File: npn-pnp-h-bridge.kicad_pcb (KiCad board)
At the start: 2 copper layers, 44.2 x 18.4 mm, 35 parts, among them J1 S4B-PH-K-S_LF__SN_, J2 S2B-PH-K-S_LF__SN_, Q1 MMBT3904, Q2 MMBT3904, Q3 MMBT3904, Q4 MMBT3904

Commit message: some small touchups
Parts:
- moved C1 1.00 mm to (151.2, 91.5)
- moved C2 1.00 mm to (155.6, 91.5)
- moved R1 1.00 mm to (153.4, 91.5)
- moved R2 1.00 mm to (157.8, 91.5)
- moved R3 1.00 mm to (160.2, 91.5)
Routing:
- net /bQ2: track 9.85 -> 8.91 mm
- net VDD: track 52.5 -> 53.1 mm
- net GND: vias 14 -> 20

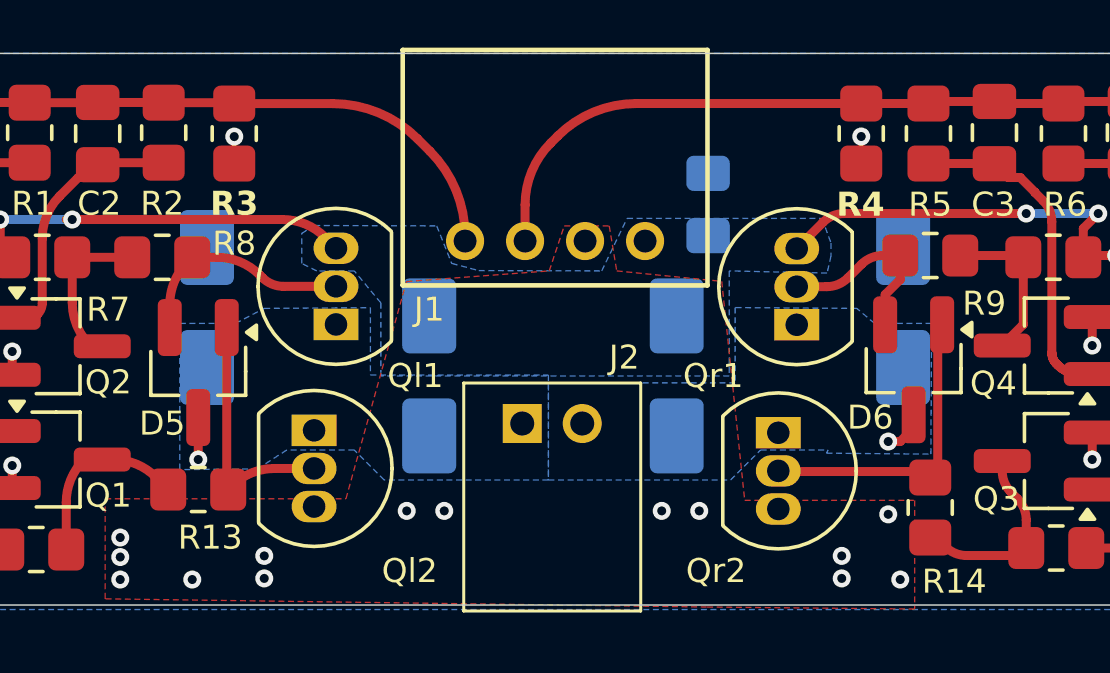
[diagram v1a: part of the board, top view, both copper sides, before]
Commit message: Use handsoldering-footprints for diodes
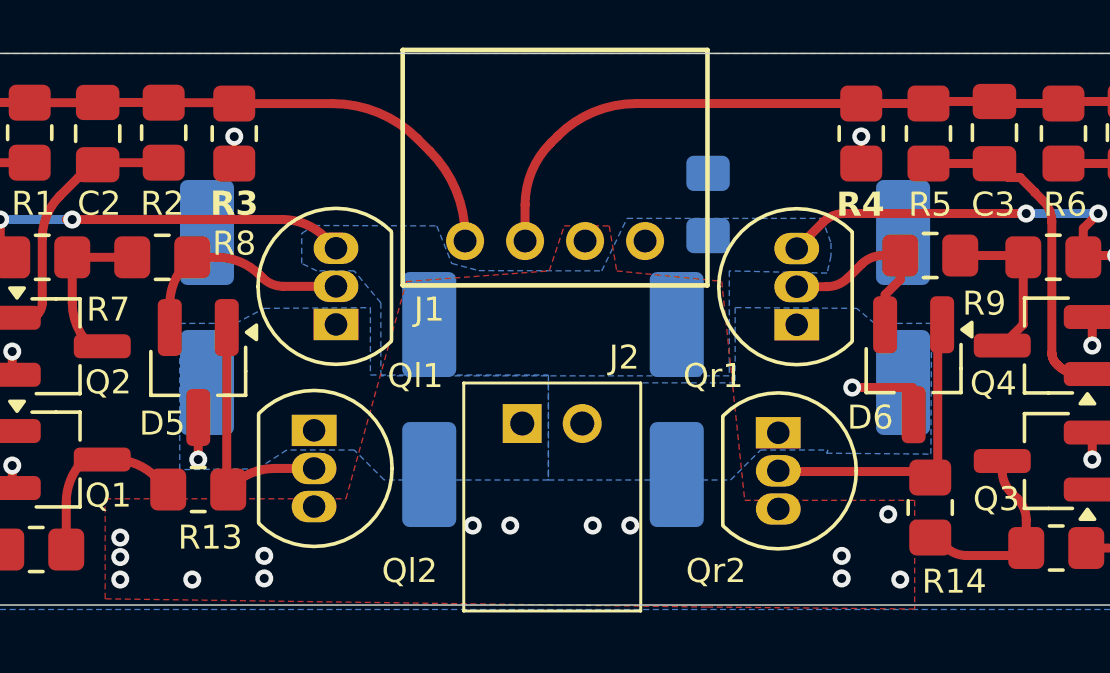
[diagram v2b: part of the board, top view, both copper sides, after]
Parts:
- D1, D2, D3, D4: footprint Diode_SMD:D_SMA -> Diode_SMD:D_SMA_Handsoldering
- moved D1 0.79 mm to (166.7, 100.4)
- moved D2 0.79 mm to (174.9, 100.4)
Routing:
- net /O2: track 1.65 -> 2.88 mm

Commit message: beautify schematic
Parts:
- added MH1: ToolingHole_1.152mm, MountingHole:ToolingHole_1.152mm, F.Cu at (162.8, 92.2)
- added MH2: ToolingHole_1.152mm, MountingHole:ToolingHole_1.152mm, F.Cu at (178.6, 92.2)
- R13, R14: value 180 -> 100
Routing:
- net /L_IN: track 19.4 -> 20.4 mm
- net /R_IN: track 23.2 -> 24.0 mm

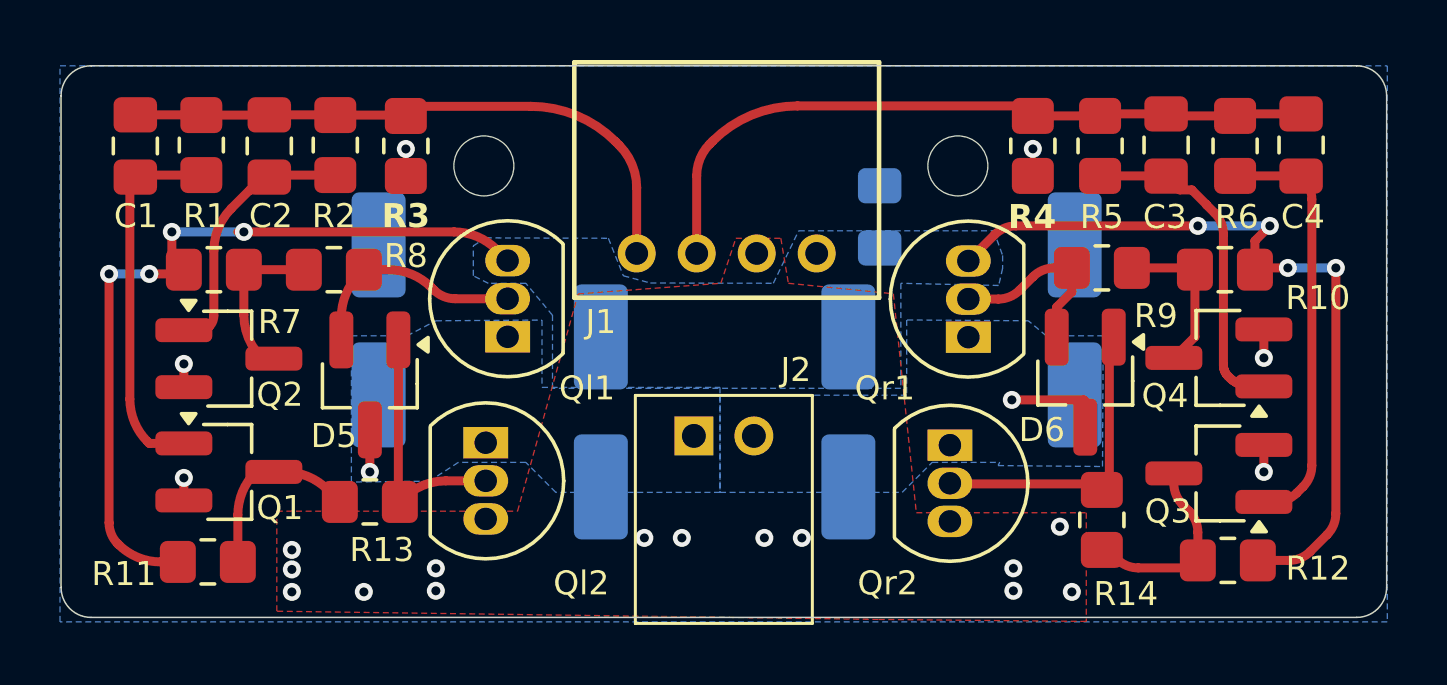
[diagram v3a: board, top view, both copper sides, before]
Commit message: Changed MMBT3904 for a dual-NPN MMDT3904 for miniturization
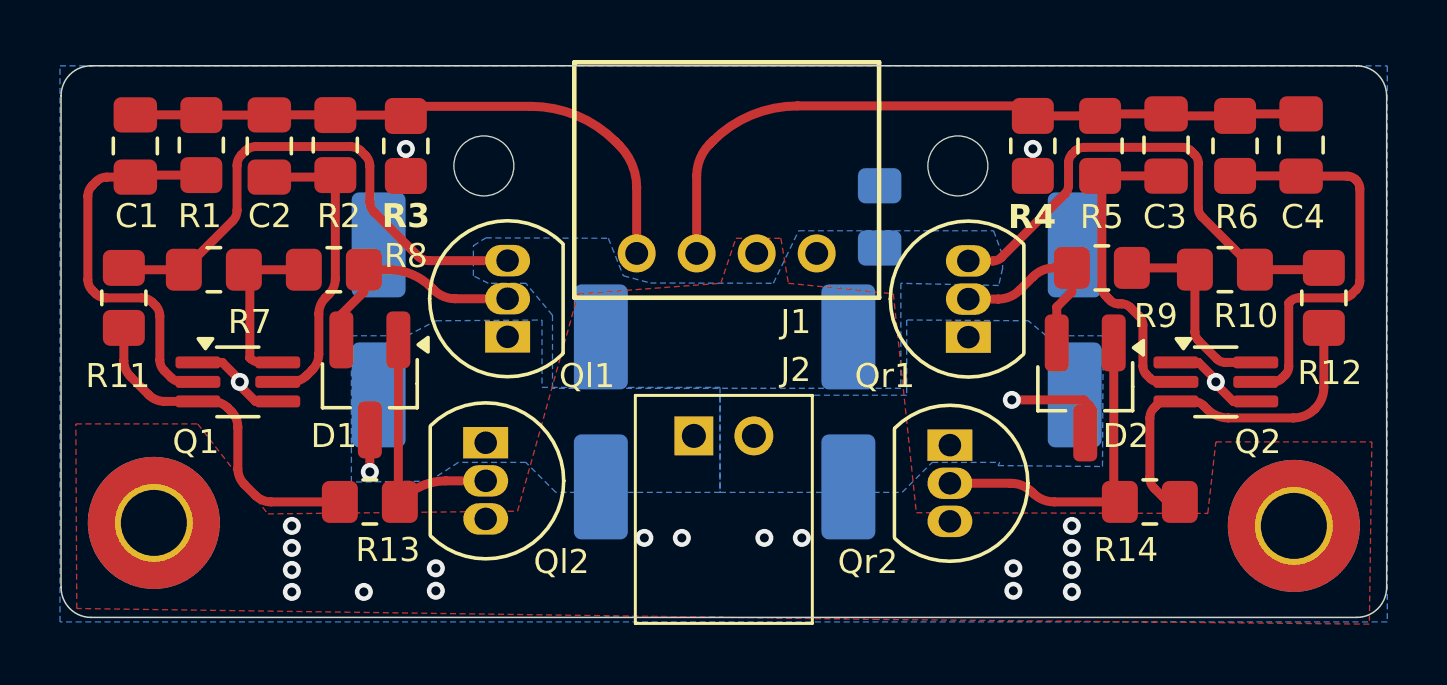
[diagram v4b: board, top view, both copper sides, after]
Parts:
- removed Q3, Q4: MMBT3904, Package_TO_SOT_SMD:SOT-23_Handsoldering
- added H1: MountingHole_Pad, MountingHole:MountingHole_2.2mm_M2_Pad_TopBottom, F.Cu at (151.8, 104.1)
- added H2: MountingHole_Pad, MountingHole:MountingHole_2.2mm_M2_Pad_TopBottom, F.Cu at (189.8, 104.2)
- Q1, Q2: value MMBT3904 -> MMDT3904; footprint Package_TO_SOT_SMD:SOT-23_Handsoldering -> Package_TO_SOT_SMD:SOT-363_SC-70-6_Handsoldering
- moved Q2 32.9 mm to (187.2, 99.4)
- moved R12 9.32 mm to (190.8, 96.6), turned to 90 degrees
- moved R11 9.23 mm to (150.8, 96.6), turned to 90 degrees
- moved C1 4.47 mm to (151.2, 91.5)
- moved C2 4.47 mm to (155.6, 91.5)
- moved R1 4.47 mm to (153.4, 91.5)
- moved R2 4.47 mm to (157.8, 91.5)
- moved Q1 3.01 mm to (154.6, 99.4)
- moved R14 1.71 mm to (185.0, 103.4), turned to 0 degrees
- moved D2 0.19 mm to (182.8, 99.6)
- renumbered C2 to C1, C1 to C2, D5 to D1, D6 to D2, D4 to D3, D3 to D4, D2 to D5, D1 to D6, R2 to R1, R1 to R2
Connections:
- Q1 pad 1: /bQ1 -> GND
- Q1 pad 2: GND -> /bQ2
- Q2 pad 1: /bQ2 -> GND
- Q2 pad 2: GND -> /bQ4
- Q2 pad 3: Net-(Q2-C) -> Net-(Q2B-C2)
- R10 pad 1: Net-(Q4-C) -> Net-(Q2A-C1)
- R12 pad 1: Net-(Q3-C) -> Net-(Q2B-C2)
- R14 pad 2: Net-(Q3-C) -> Net-(Q2B-C2)
- R7 pad 1: Net-(Q2-C) -> Net-(Q1A-C1)
- R8 pad 1: Net-(Q2-C) -> Net-(Q1A-C1)
- R9 pad 2: Net-(Q4-C) -> Net-(Q2A-C1)
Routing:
- net VDD: track 53.1 -> 34.7 mm, vias 8 -> 0
- net Net-(Q2B-C2): track 0.00 -> 12.2 mm
- net Net-(Q2A-C1): track 0.00 -> 6.71 mm
- net Net-(Q3-C): track 6.64 -> 0.00 mm
- net Net-(Q1A-C1): track 0.00 -> 5.97 mm
- net Net-(Q2-C): track 5.50 -> 0.00 mm
- net Net-(Q4-C): track 5.36 -> 0.00 mm
- net Net-(Q1B-C2): track 6.27 -> 11.4 mm
- net /bQ2: track 8.91 -> 13.1 mm
- net GND: track 5.17 -> 8.39 mm, vias 20 -> 21
- net /bQ1: track 12.5 -> 10.2 mm
- net /L2b: track 10.4 -> 11.2 mm
- net /bQ3: track 14.2 -> 13.7 mm

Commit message: fine tuning
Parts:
- moved J1 0.92 mm to (173.9, 94.2)
- moved R14 0.80 mm to (184.2, 103.4)
- moved J2 0.80 mm to (169.8, 102.0)
- moved C5 0.33 mm to (176.2, 93.6)
- moved MH1 0.20 mm to (162.6, 92.2)
- moved MH2 0.20 mm to (178.8, 92.2)
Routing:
- net /O2: track 3.28 -> 1.93 mm
- net /R_IN: track 24.0 -> 23.1 mm
- net /L_IN: track 20.4 -> 19.5 mm
- net Net-(Q2B-C2): track 12.2 -> 11.7 mm
- net GND: vias 21 -> 18

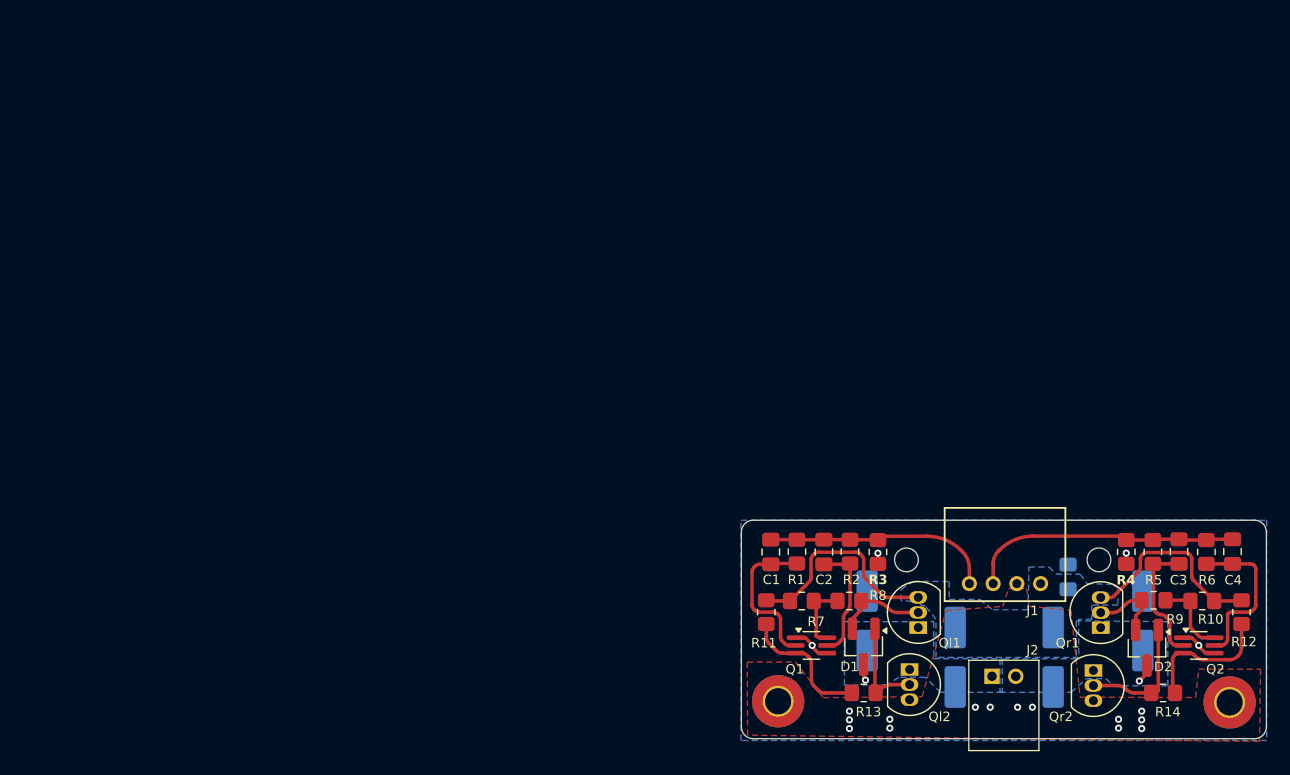
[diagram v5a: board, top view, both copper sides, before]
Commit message: more fine tuning; round board size
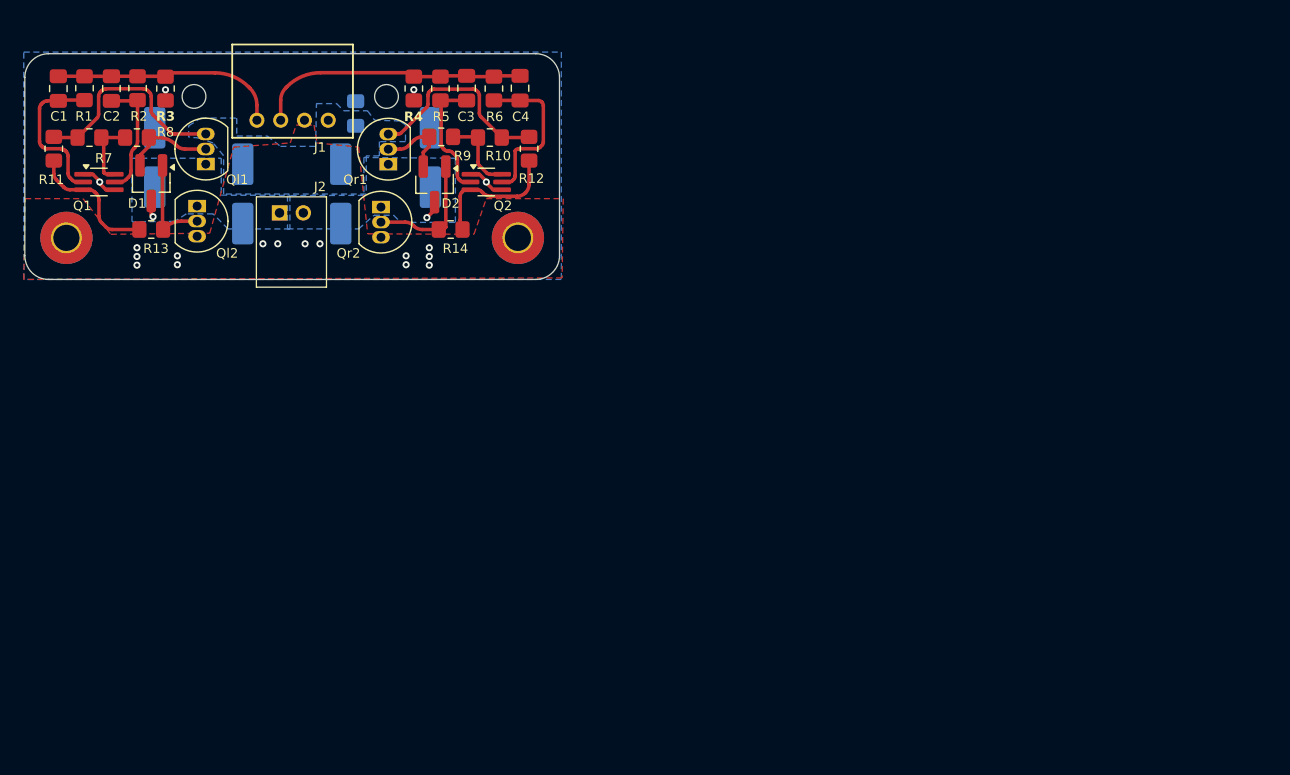
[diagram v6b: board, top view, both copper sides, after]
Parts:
- moved H2 71.5 mm to (129.9, 65.1)
- moved C3 71.5 mm to (125.6, 52.5)
- moved J2 71.5 mm to (109.8, 63.0)
- moved MH2 71.5 mm to (118.8, 53.2)
- moved C1 71.5 mm to (91.2, 52.5)
- moved C2 71.5 mm to (95.7, 52.5)
- moved C4 71.5 mm to (130.1, 52.5)
- moved D1 71.5 mm to (99.0, 60.5)
- moved D3 71.5 mm to (122.5, 58.3)
- moved MH1 71.5 mm to (102.6, 53.2)
- moved Q1 71.5 mm to (94.6, 60.4)
- moved Ql1 71.5 mm to (103.6, 58.9)
- moved R10 71.5 mm to (127.5, 56.7)
- moved R11 71.5 mm to (90.8, 57.6)
- moved R12 71.5 mm to (130.8, 57.6)
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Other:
- board size 44.2 x 18.4 mm -> 45 x 19 mm

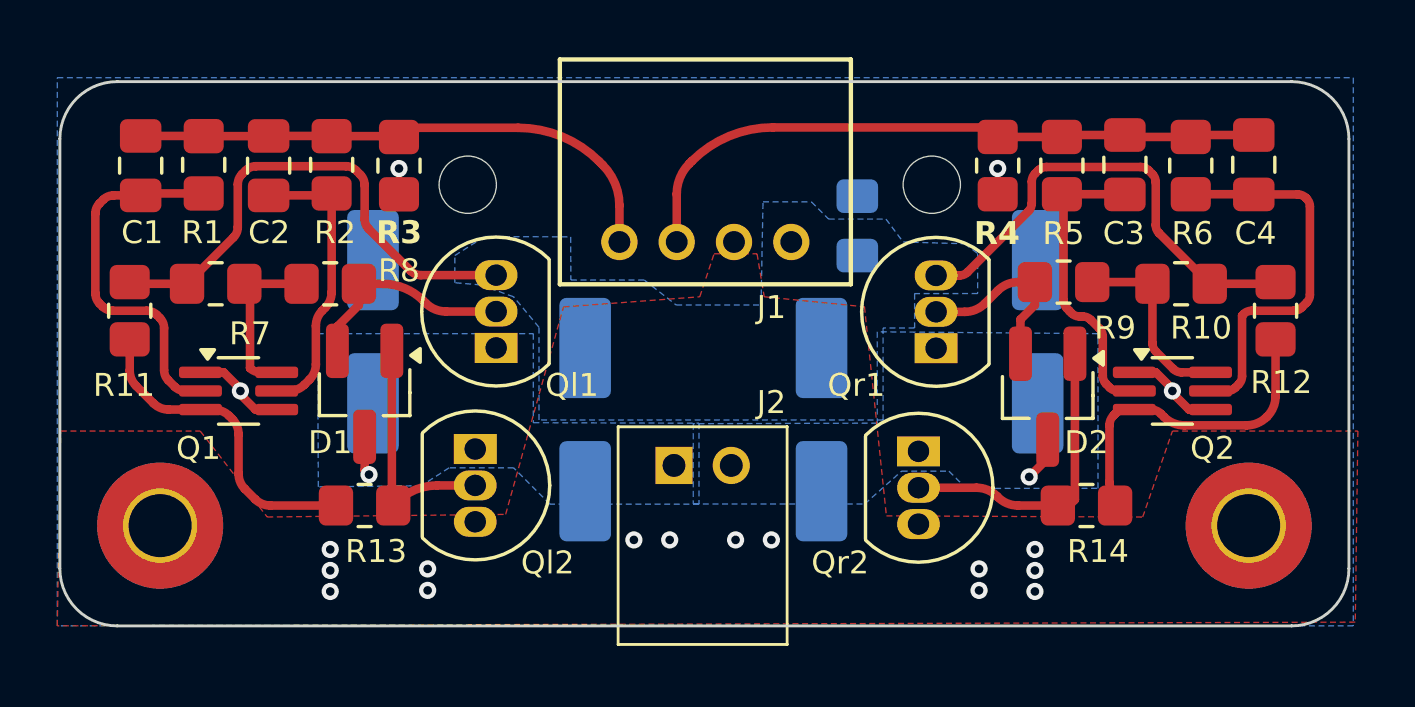
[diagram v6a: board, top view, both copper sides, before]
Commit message: final touches for dual-npn-package
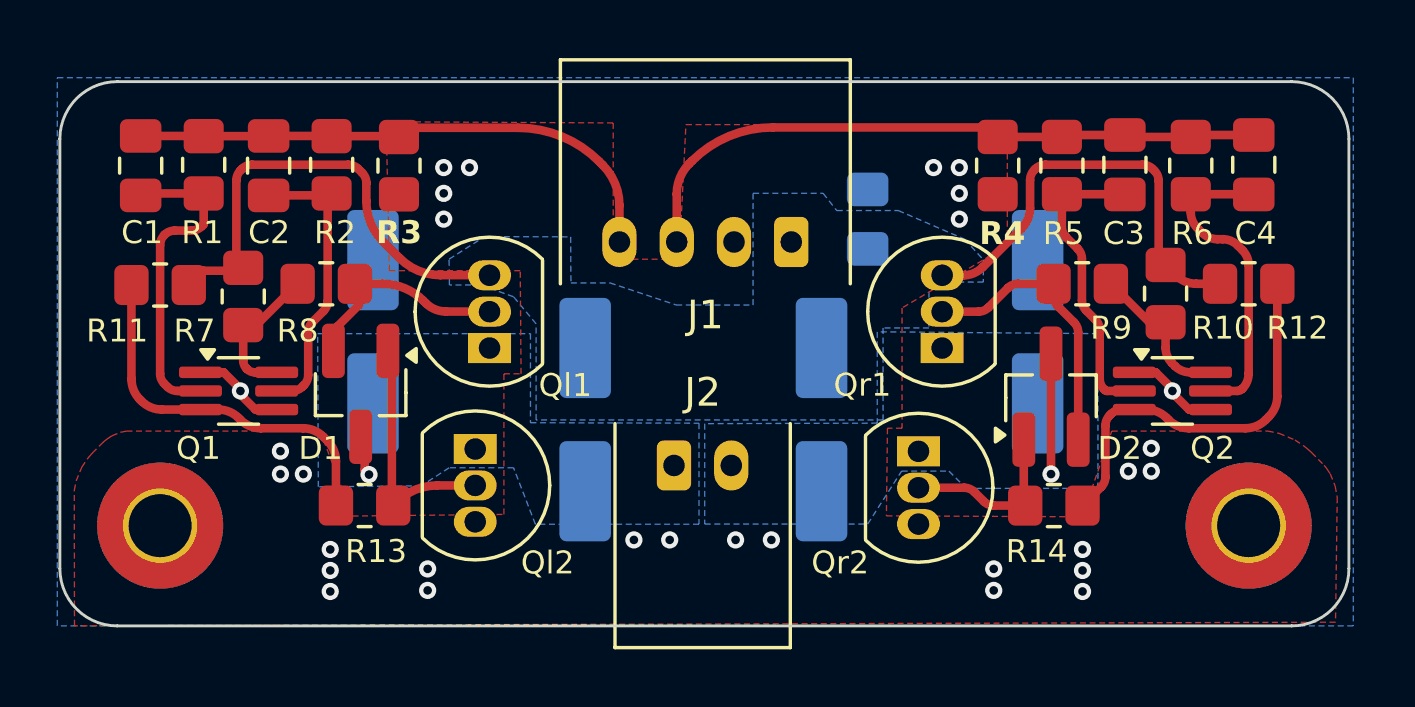
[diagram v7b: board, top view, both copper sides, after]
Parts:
- removed MH1, MH2: ToolingHole_1.152mm, MountingHole:ToolingHole_1.152mm
- J1: footprint Misc:CONN_S4B-PH-K-S_JST -> Misc:JST_PH_S4B-PH-K_1x04_P2.00mm_Horizontal
- J2: footprint Misc:DS2BPHKSLFSN -> Misc:JST_PH_S2B-PH-K_1x02_P2.00mm_Horizontal
- moved R11 1.39 mm to (91.9, 56.7), turned to 0 degrees
- moved R12 1.33 mm to (129.9, 56.7), turned to 180 degrees
- moved R14 1.14 mm to (123.1, 64.4)
- moved R7 1.06 mm to (94.8, 57.1), turned to 90 degrees
- moved R9 0.65 mm to (124.1, 56.7)
- moved R10 0.64 mm to (127.0, 57.0), turned to 90 degrees
- moved C5 0.43 mm to (116.6, 54.4)
- moved Ql1 0.23 mm to (103.4, 58.9)
- moved Qr1 0.21 mm to (119.2, 58.9)
- moved D1 0.14 mm to (98.9, 60.5)
- moved R8 0.14 mm to (97.7, 56.7)
- moved D2 0.12 mm to (123.0, 60.6), turned to 90 degrees
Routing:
- net /L2b: track 10.8 -> 6.26 mm
- net /H2b: track 6.49 -> 9.99 mm
- net VDD: track 34.7 -> 32.2 mm
- net Net-(Q2B-C2): track 11.7 -> 14.1 mm
- net /bQ3: track 13.7 -> 11.3 mm
- net /O2: track 1.93 -> 4.20 mm
- net Net-(Q1B-C2): track 11.4 -> 13.4 mm
- net GND: track 8.39 -> 6.69 mm, vias 18 -> 30
- net /bQ2: track 13.1 -> 11.4 mm
- net Net-(Q2A-C1): track 6.71 -> 5.39 mm
- net Net-(Q1A-C1): track 5.97 -> 5.13 mm
